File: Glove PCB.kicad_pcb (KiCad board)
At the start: 2 copper layers, 35 x 35 mm, 103 parts, among them IC2 MAX11128ATI+, IC3 MAX11128ATI+, J1 USB_B_Micro, J2 Conn_01x08_Female, J3 Conn_01x08_Female, J4 Conn_01x02_Female, J5 Conn_01x02_Female, J6 Conn_01x02_Female, Q1 DMG2305, Q2 BSS138, Q3 BSS138, U1 MCP73831T-2ACI_OT, U2 REF3030, U3 113990582

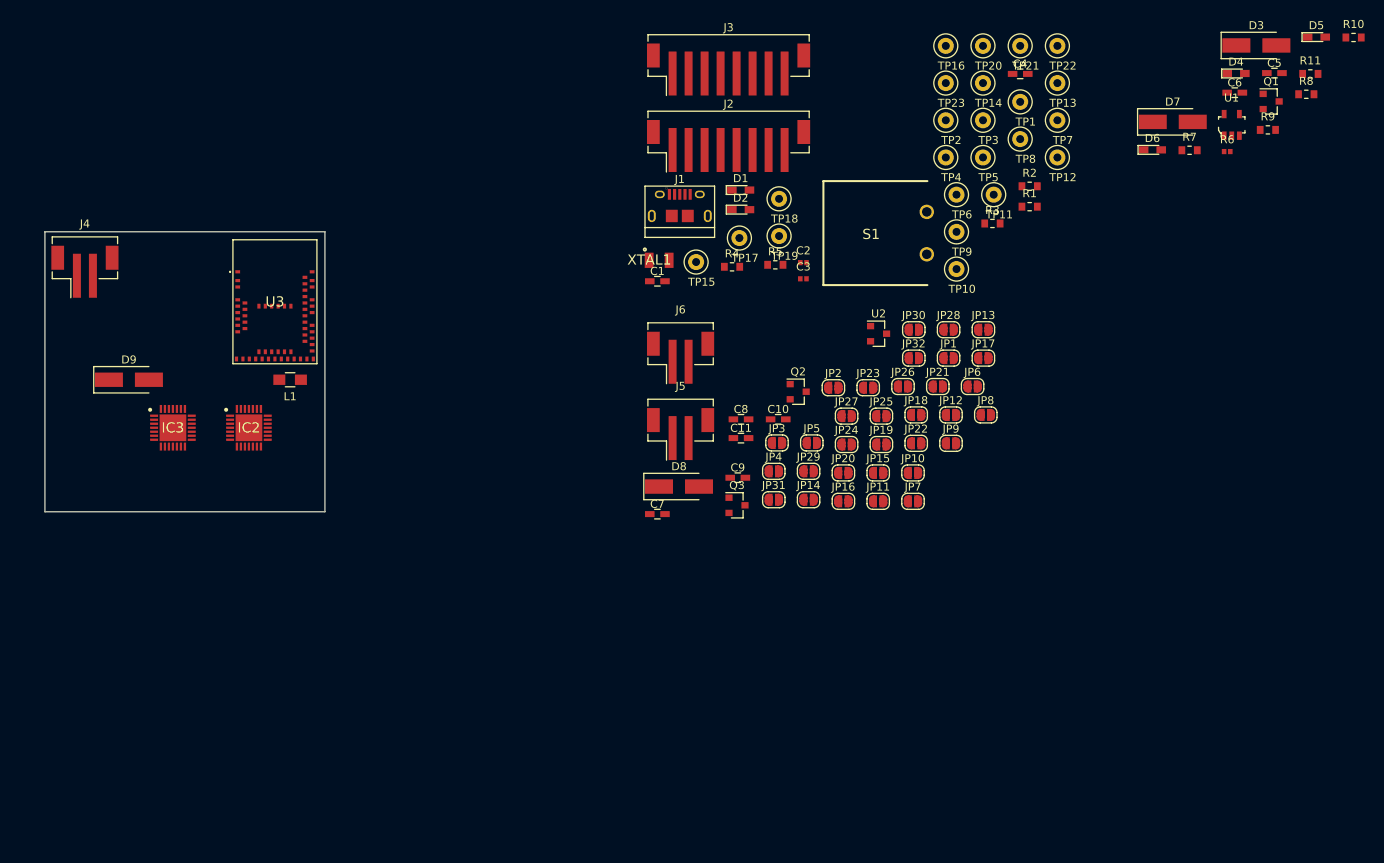
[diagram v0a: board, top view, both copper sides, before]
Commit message: Added project and digikey footprints. Added mini-spox connectors.
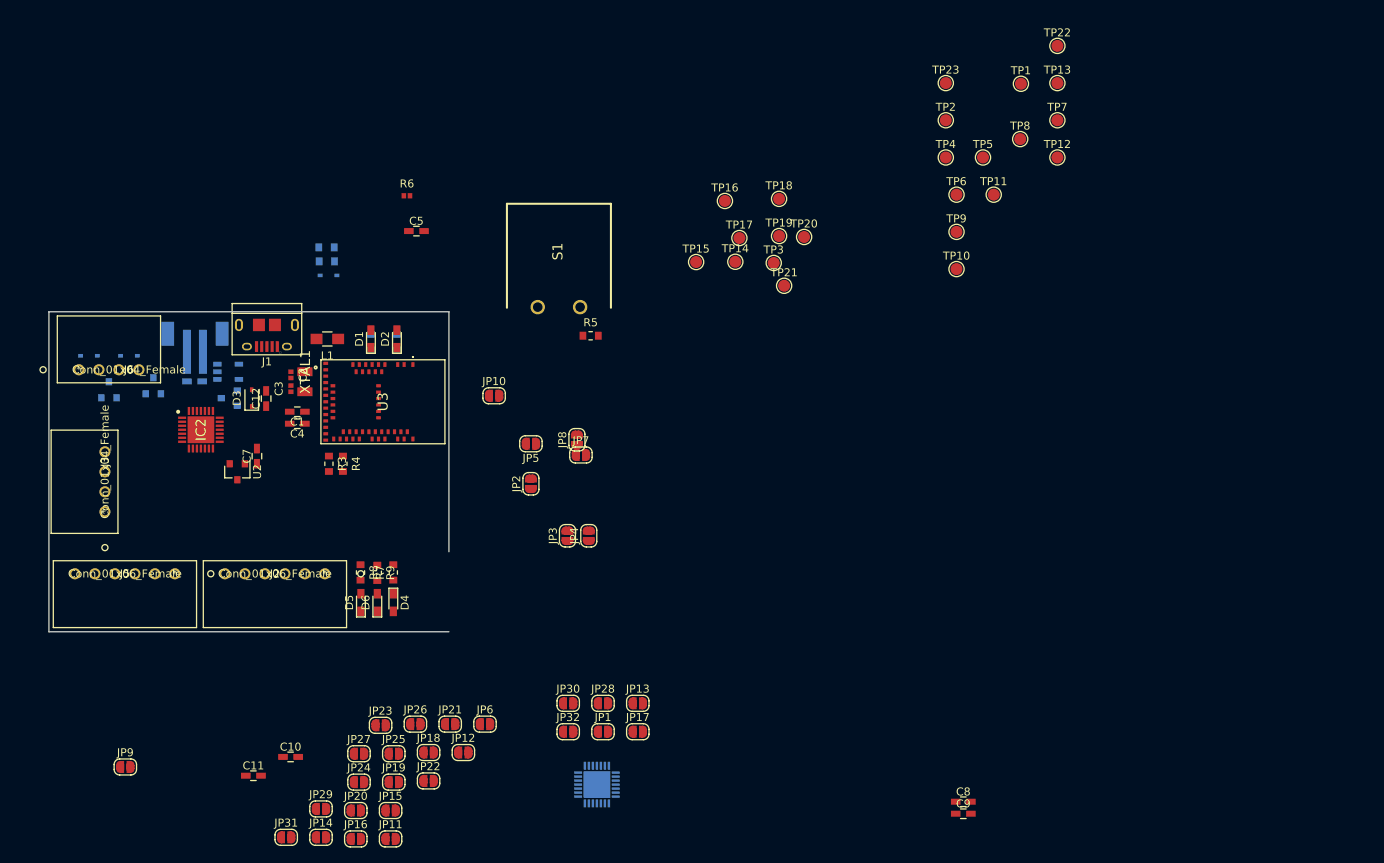
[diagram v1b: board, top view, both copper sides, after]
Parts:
- added C12: 10uF, Capacitors_SMD:C_0603_HandSoldering, F.Cu at (47.1, 165.8)
- C6, IC3, J4, Q1, Q2, Q3, R1, R10, R11, R2, U1: moved to B.Cu
- C7: value 0.1u -> 0.47u
- D3: value SS54 -> 1N5819WS; footprint Diode_SMD:D_SMA_Handsoldering -> Diode_SMD:D_SOD-323
- D7, D8, D9: value SS54 -> 1N5819WS; footprint Diode_SMD:D_SMA_Handsoldering -> Diode_SMD:D_SOD-323; moved to B.Cu
- J2: value Conn_01x08_Female -> Conn_01x06_Female; footprint Connectors_JST:JST_PH_B8B-PH-SM4-TB_08x2.00mm_Straight -> Glove-PCB:22-05-7065
- J3: value Conn_01x08_Female -> Conn_01x04_Female; footprint Connectors_JST:JST_PH_B8B-PH-SM4-TB_08x2.00mm_Straight -> Glove-PCB:22-05-7045
- J5: value Conn_01x02_Female -> Conn_01x06_Female; footprint Connector_JST:JST_PH_B2B-PH-SM4-TB_1x02_P2.00mm_Vertical -> Glove-PCB:22-05-7065
- J6: value Conn_01x02_Female -> Conn_01x04_Female; footprint Connector_JST:JST_PH_B2B-PH-SM4-TB_1x02_P2.00mm_Vertical -> Glove-PCB:22-05-7045
- TP1, TP10, TP11, TP12, TP13, TP14, TP15, TP16, TP17, TP18, TP19, TP2, TP20, TP21, TP22, TP23, TP3, TP4, TP5, TP6, TP7, TP8, TP9: footprint TestPoint:TestPoint_Loop_D1.80mm_Drill1.0mm_Beaded -> TestPoint:TestPoint_Pad_D1.5mm
- moved D5 138.8 mm to (59.0, 191.3), turned to 90 degrees
- moved Q1 135.4 mm to (42.5, 165.8), turned to 180 degrees
- moved C6 134.9 mm to (38.2, 163.7), turned to 180 degrees
- moved D3 133.1 mm to (45.4, 165.8), turned to 90 degrees
- moved R8 132.5 mm to (59.0, 187.6), turned to 270 degrees
- moved R10 131.4 mm to (54.7, 148.7), turned to 180 degrees
- moved U1 129.2 mm to (42.4, 162.5), turned to 90 degrees
- moved R11 124.9 mm to (54.7, 146.9)
- moved D4 124.4 mm to (63.0, 191.3), turned to 270 degrees
- moved R9 124.3 mm to (61.0, 187.6), turned to 270 degrees
- moved R7 112.7 mm to (63.0, 187.6), turned to 90 degrees
- moved D6 112.2 mm to (61.0, 191.3), turned to 90 degrees
- moved JP9 110.9 mm to (29.6, 211.9)
- moved C5 109.1 mm to (65.9, 144.9)
- moved D7 107.3 mm to (55.0, 150.4)
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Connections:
- C7 pad 1: /AREF -> +3V3
- D8 pad 2: Net-(D8-Pad2) -> /Sensors/HapticN_0
- D9 pad 2: Net-(D9-Pad2) -> /Sensors/HapticN_1
- J3 pad 1: /Sensors/A8 -> /Sensors/A6
- J3 pad 2: /Sensors/A9 -> /Sensors/A7
- J3 pad 3: /Sensors/A10 -> /Sensors/A8
- J3 pad 4: /Sensors/A11 -> /Sensors/A9
- J5 pad 1: +3V3 -> /Sensors/A10
- J5 pad 2: Net-(D8-Pad2) -> /Sensors/A11
- J6 pad 2: Net-(D9-Pad2) -> /Sensors/HapticN_0
- Q2 pad 3: Net-(D8-Pad2) -> /Sensors/HapticN_0
- Q3 pad 3: Net-(D9-Pad2) -> /Sensors/HapticN_1
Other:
- board size 35 x 35 mm -> 50 x 40 mm

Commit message: Placement done. Started layout.
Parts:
- removed JP1, JP10, JP11, JP12, JP13, JP14, JP15, JP16, JP17, JP18, JP19, JP2, JP20, JP21, JP22, JP23, JP24, JP25, JP26, JP27, JP28, JP29, JP3, JP30, JP31, JP32, JP4, JP5, JP6, JP7, JP8, JP9: SolderJumper_2_Open, Jumper:SolderJumper-2_P1.3mm_Open_RoundedPad1.0x1.5mm
- removed S1: GPTS203211B, SamacSys_Parts:GPTS203211B
- removed the TP2 at (132.1, 131.1)
- removed TP21: AREF, TestPoint:TestPoint_Pad_D1.5mm
- removed the TP3 at (110.6, 148.9)
- removed the TP4 at (132.1, 135.7)
- removed the TP5 at (136.8, 135.7)
- removed the TP6 at (133.4, 140.4)
- removed the TP7 at (146.1, 131.1)
- removed the TP8 at (141.4, 133.4)
- added C13: 0.1u, Capacitors_SMD:C_0603_HandSoldering, B.Cu at (41.6, 173.4)
- added C14: 10u, Capacitors_SMD:C_0603_HandSoldering, B.Cu at (41.6, 172.1)
- added C15: 0.1u, Capacitors_SMD:C_0603_HandSoldering, B.Cu at (46.5, 175.2)
- added C16: 10u, Capacitors_SMD:C_0603_HandSoldering, B.Cu at (47.8, 175.2)
- added SW1: TS-1109S-B-B, Glove-PCB:Button, F.Cu at (51.5, 177.5)
- added TP15: AREF, TestPoint:TestPoint_Pad_D1.5mm, F.Cu at (40.2, 170.0)
- D7, R10, R11: moved to F.Cu
- R6: moved to B.Cu
- moved TP1 122.8 mm to (32.0, 167.4)
- moved C9 108.2 mm to (37.1, 170.2)
- moved C8 107.0 mm to (37.1, 171.4)
- moved TP2 105.8 mm to (34.5, 167.4)
- moved TP6 94.2 mm to (63.5, 181.0)
- moved TP16 89.0 mm to (58.5, 158.4)
- moved TP3 78.7 mm to (62.5, 178.9)
- moved TP4 78.6 mm to (61.2, 180.8)
- moved TP5 64.6 mm to (89.9, 183.4)
- moved TP7 64.6 mm to (97.9, 169.5)
- moved TP14 63.6 mm to (60.1, 178.8)
- moved TP13 62.1 mm to (58.1, 177.7)
- moved TP12 60.5 mm to (62.4, 176.6)
- moved IC3 58.8 mm to (42.7, 177.3), turned to 90 degrees
- moved TP10 56.0 mm to (59.0, 173.9)
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- renumbered TP22 to TP1, TP16 to TP10, TP17 to TP11, TP18 to TP12, TP19 to TP13, TP20 to TP14, TP1 to TP16, TP23 to TP2, TP9 to TP3, TP10 to TP4, TP11 to TP5, TP12 to TP6, TP13 to TP7, TP14 to TP8, TP15 to TP9
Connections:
- net Net-(TP10-Pad1) renamed /SWDIO
- net Net-(TP11-Pad1) renamed /NFC1
- net Net-(TP12-Pad1) renamed /SWDCLK
- net Net-(TP13-Pad1) renamed /NFC2
- net Net-(TP9-Pad1) renamed /SWDI
- IC2 pad 10: /Sensors/AIN12_0 -> /Sensors/A12
- IC2 pad 11: /Sensors/AIN13_0 -> /Sensors/A13
- IC2 pad 12: /Sensors/AIN14_0 -> /Sensors/A14
- IC2 pad 13: /Sensors/AIN15_0 -> /Sensors/A15
- IC2 pad 6: /Sensors/AIN8_0 -> /Sensors/A8
- IC2 pad 7: /Sensors/AIN9_0 -> /Sensors/A9
- IC2 pad 8: /Sensors/AIN10_0 -> /Sensors/A10
- IC2 pad 9: /Sensors/AIN11_0 -> /Sensors/A11
- IC3 pad 10: /Sensors/AIN12_1 -> /Sensors/A12
- IC3 pad 11: /Sensors/AIN13_1 -> /Sensors/A13
- IC3 pad 12: /Sensors/AIN14_1 -> /Sensors/A14
- IC3 pad 13: /Sensors/AIN15_1 -> /Sensors/A15
- IC3 pad 6: /Sensors/AIN8_1 -> /Sensors/A8
- IC3 pad 7: /Sensors/AIN9_1 -> /Sensors/A9
- IC3 pad 8: /Sensors/AIN10_1 -> /Sensors/A10
- IC3 pad 9: /Sensors/AIN11_1 -> /Sensors/A11
- U3 pad 11: /AREF -> Net-(U3-Pad11)
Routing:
- net +3V3: track 0.00 -> 7.01 mm
- net /Sensors/HapticN_1: track 0.00 -> 4.54 mm
- net /Sensors/HapticN_0: track 0.00 -> 4.03 mm
- net VBUS: track 0.00 -> 3.76 mm, vias 0 -> 4
- net /H0: track 0.00 -> 0.65 mm
- net VDD: vias 0 -> 4
- net (no net): vias 0 -> 22
- added copper zone on B.Cu, net (none)
- added copper zone on F.Cu, net (none)
- added copper zone on B.Cu, net +BATT
- added copper zone on F.Cu, net VBUS
- added copper zone on B.Cu, net VDD
- added copper zone on F.Cu, net VDD
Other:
- outline, holes or cut-outs redrawn
- net class Default: via_dia 0.8 -> 0.6; via_drill 0.4 -> 0.3

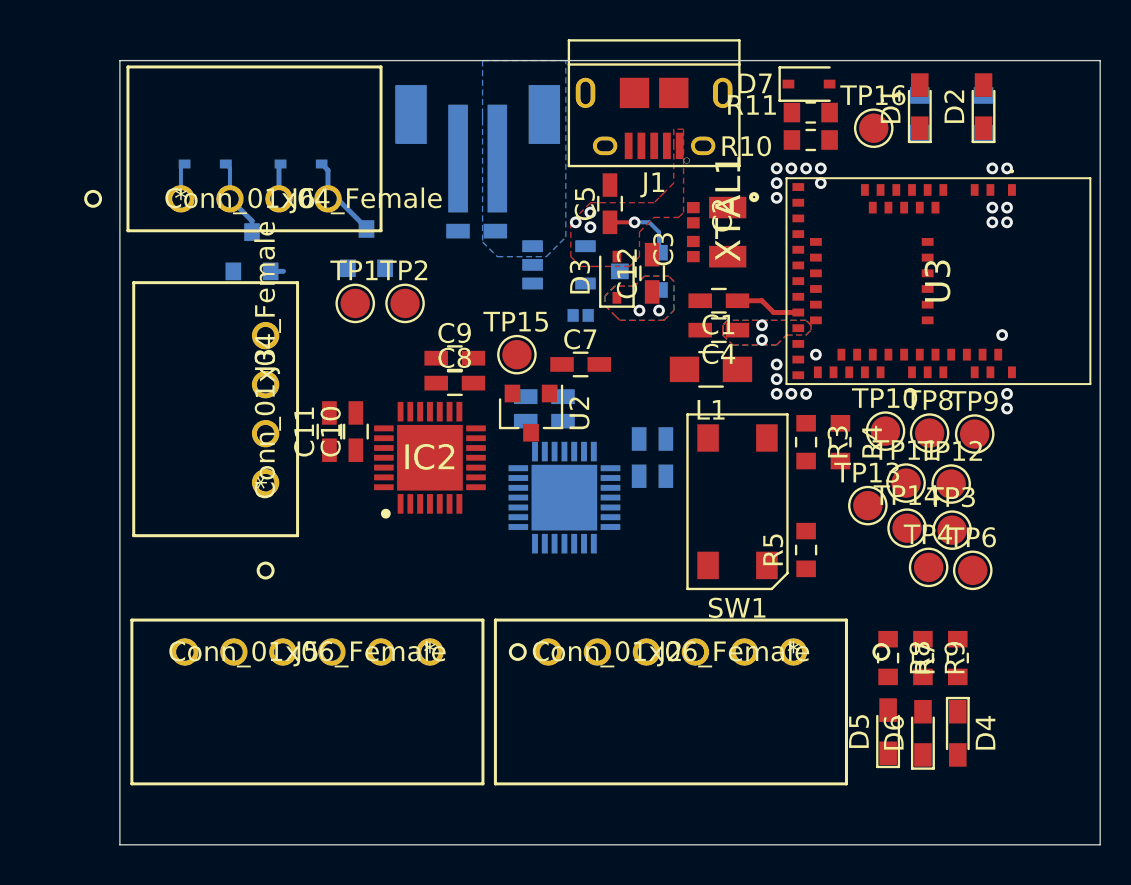
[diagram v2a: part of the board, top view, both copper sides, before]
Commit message: Changed to 4-layer board, added power shapes in layout.
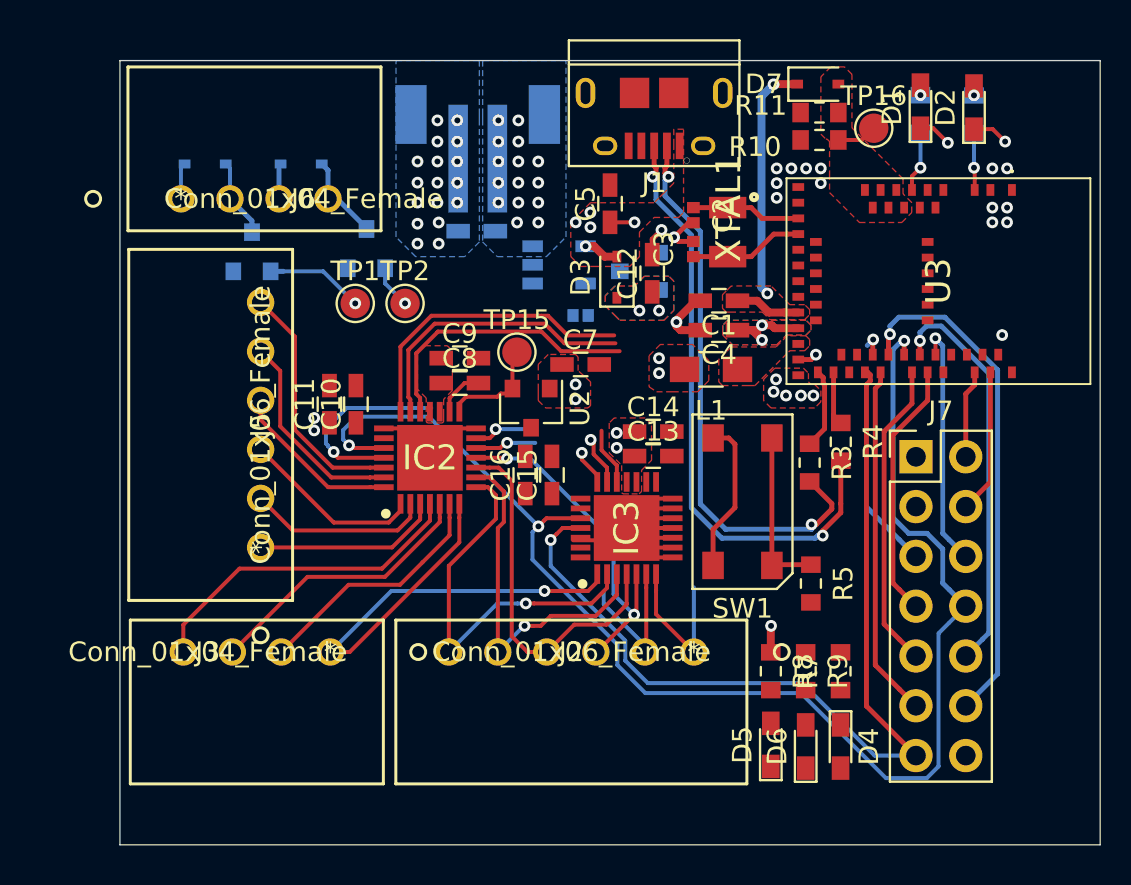
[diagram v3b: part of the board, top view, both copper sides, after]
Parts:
- removed TP10: SCK, TestPoint:TestPoint_Pad_D1.5mm
- removed TP11: ~CS0, TestPoint:TestPoint_Pad_D1.5mm
- removed TP12: ~CS1, TestPoint:TestPoint_Pad_D1.5mm
- removed TP13: ~EOC0, TestPoint:TestPoint_Pad_D1.5mm
- removed TP14: EOC1, TestPoint:TestPoint_Pad_D1.5mm
- removed TP3: SWDI, TestPoint:TestPoint_Pad_D1.5mm
- removed TP4: SWDIO, TestPoint:TestPoint_Pad_D1.5mm
- removed TP6: SWDCLK, TestPoint:TestPoint_Pad_D1.5mm
- removed TP8: MISO, TestPoint:TestPoint_Pad_D1.5mm
- removed TP9: MOSI, TestPoint:TestPoint_Pad_D1.5mm
- added J7: Conn_02x07_Odd_Even, Connector_PinHeader_2.54mm:PinHeader_2x07_P2.54mm_Vertical, F.Cu at (60.6, 175.2)
- C13, C14, C15, C16, IC3: moved to F.Cu
- C2, C3: value 12pF -> 18pF
- XTAL1: value ECS-_327-12_5-34B-TR -> Q13FC1350000400
- moved J5 10.2 mm to (27.2, 179.8), turned to 90 degrees
- moved J3 9.25 mm to (30.7, 185.2), turned to 180 degrees
- moved C16 7.22 mm to (40.7, 176.1)
- moved D5 6.02 mm to (53.2, 189.9)
- moved D6 6.02 mm to (55.0, 190.0)
- moved R8 6.02 mm to (53.2, 186.1)
- moved R9 6.02 mm to (55.0, 186.1)
- moved D4 6.02 mm to (56.8, 190.0)
- moved R7 6.02 mm to (56.8, 186.1)
- moved C13 5.83 mm to (47.2, 175.2), turned to 0 degrees
- moved C14 5.83 mm to (47.2, 173.9), turned to 0 degrees
- moved J2 5.08 mm to (49.3, 185.2)
- moved C15 4.53 mm to (42.0, 176.1)
- moved IC3 3.53 mm to (45.8, 178.8)
- moved R5 1.73 mm to (55.2, 181.7), turned to 270 degrees
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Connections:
- net Net-(J1-Pad2) renamed /D-
- net Net-(J1-Pad3) renamed /D+
- net Net-(R3-Pad1) renamed /nRF_D-
- net Net-(R4-Pad1) renamed /nRF_D+
- net Net-(SW1-Pad1) renamed /RST
- IC2 pad 1: /Sensors/A3 -> /Sensors/A12
- IC2 pad 10: /Sensors/A12 -> /Sensors/A3
- IC2 pad 11: /Sensors/A13 -> /Sensors/A2
- IC2 pad 12: /Sensors/A14 -> /Sensors/A1
- IC2 pad 13: /Sensors/A15 -> /Sensors/A0
- IC2 pad 2: /Sensors/A4 -> /Sensors/A11
- IC2 pad 26: /Sensors/A0 -> /Sensors/A15
- IC2 pad 27: /Sensors/A1 -> /Sensors/A14
- IC2 pad 28: /Sensors/A2 -> /Sensors/A13
- IC2 pad 3: /Sensors/A5 -> /Sensors/A10
- IC2 pad 4: /Sensors/A6 -> /Sensors/A9
- IC2 pad 5: /Sensors/A7 -> /Sensors/A8
- IC2 pad 6: /Sensors/A8 -> /Sensors/A7
- IC2 pad 7: /Sensors/A9 -> /Sensors/A6
- IC2 pad 8: /Sensors/A10 -> /Sensors/A5
- IC2 pad 9: /Sensors/A11 -> /Sensors/A4
- IC3 pad 1: /Sensors/A3 -> /Sensors/A6
- IC3 pad 10: /Sensors/A12 -> GND
- IC3 pad 11: /Sensors/A13 -> GND
- IC3 pad 12: /Sensors/A14 -> GND
- IC3 pad 13: /Sensors/A15 -> GND
- IC3 pad 2: /Sensors/A4 -> /Sensors/A5
- IC3 pad 26: /Sensors/A0 -> GND
- IC3 pad 27: /Sensors/A1 -> GND
- IC3 pad 28: /Sensors/A2 -> /Sensors/A7
- IC3 pad 3: /Sensors/A5 -> /Sensors/A4
- IC3 pad 4: /Sensors/A6 -> /Sensors/A3
- IC3 pad 5: /Sensors/A7 -> /Sensors/A2
- IC3 pad 6: /Sensors/A8 -> /Sensors/A1
- IC3 pad 7: /Sensors/A9 -> /Sensors/A0
- IC3 pad 8: /Sensors/A10 -> GND
- IC3 pad 9: /Sensors/A11 -> GND
- U3 pad 39: Net-(U3-Pad39) -> /~EOC1
- U3 pad 41: Net-(U3-Pad41) -> /~EOC0
- U3 pad 44: /~CS0 -> /~CS1
- U3 pad 46: /~CS1 -> /~CS0
- U3 pad 47: /SWDI -> /SWO
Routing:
- net /MISO: track 0.00 -> 71.0 mm, vias 0 -> 3
- net +3V3: track 7.01 -> 55.1 mm, vias 0 -> 11
- net /~EOC1: track 0.00 -> 47.2 mm, vias 0 -> 1
- net /SCK: track 0.00 -> 43.3 mm, vias 0 -> 1
- net GND: track 0.00 -> 41.0 mm, vias 0 -> 25
- net /MOSI: track 0.00 -> 37.8 mm, vias 0 -> 2
- net /D+: track 0.00 -> 31.1 mm, vias 0 -> 2
- net /D-: track 0.00 -> 28.9 mm, vias 0 -> 2
- net /~EOC0: track 0.00 -> 27.9 mm, vias 0 -> 1
- net /~CS0: track 0.00 -> 27.9 mm
- net /Sensors/A6: track 0.00 -> 26.4 mm, vias 0 -> 1
- net /Sensors/A5: track 0.00 -> 20.3 mm, vias 0 -> 1
- net /Sensors/A3: track 0.00 -> 18.8 mm
- net /Sensors/A4: track 0.00 -> 18.4 mm, vias 0 -> 1
- net /~CS1: track 0.00 -> 18.2 mm, vias 0 -> 1
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- added copper zone on F.Cu, net +3V3
- added copper zone on In1.Cu, net +3V3
- added copper zone on F.Cu, net /VBATT_OUT
- added copper zone on B.Cu, net GND
- added copper zone on F.Cu, net GND
- added copper zone on In2.Cu, net GND
- added copper zone on F.Cu, net Net-(L1-Pad1)
- added copper zone on In1.Cu, net VBUS
- added copper zone on In1.Cu, net VDD
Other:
- copper layers 2 -> 4
